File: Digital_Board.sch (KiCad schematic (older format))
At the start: 0 parts

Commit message: Rearranged the top sheet blocks modified hir. pins in few blocks
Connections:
- net labels added: 12V
- wire segments 23 -> 24

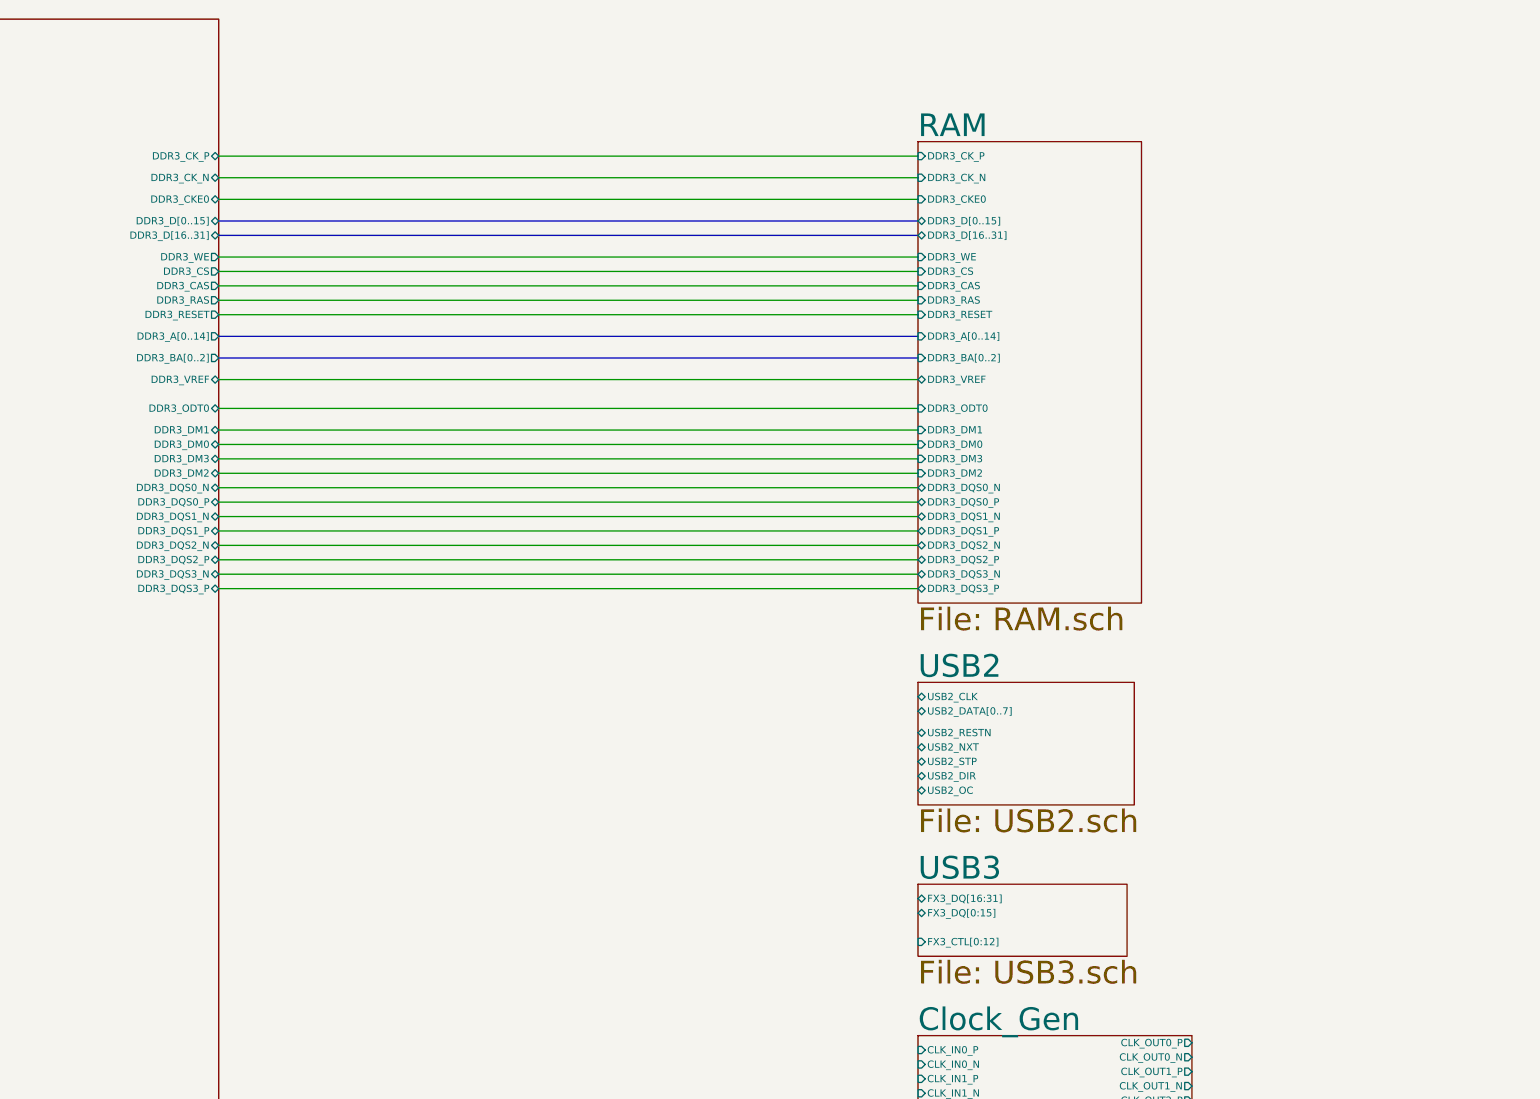
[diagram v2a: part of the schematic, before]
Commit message: Added nets for fx3 usb3 cct from fpga
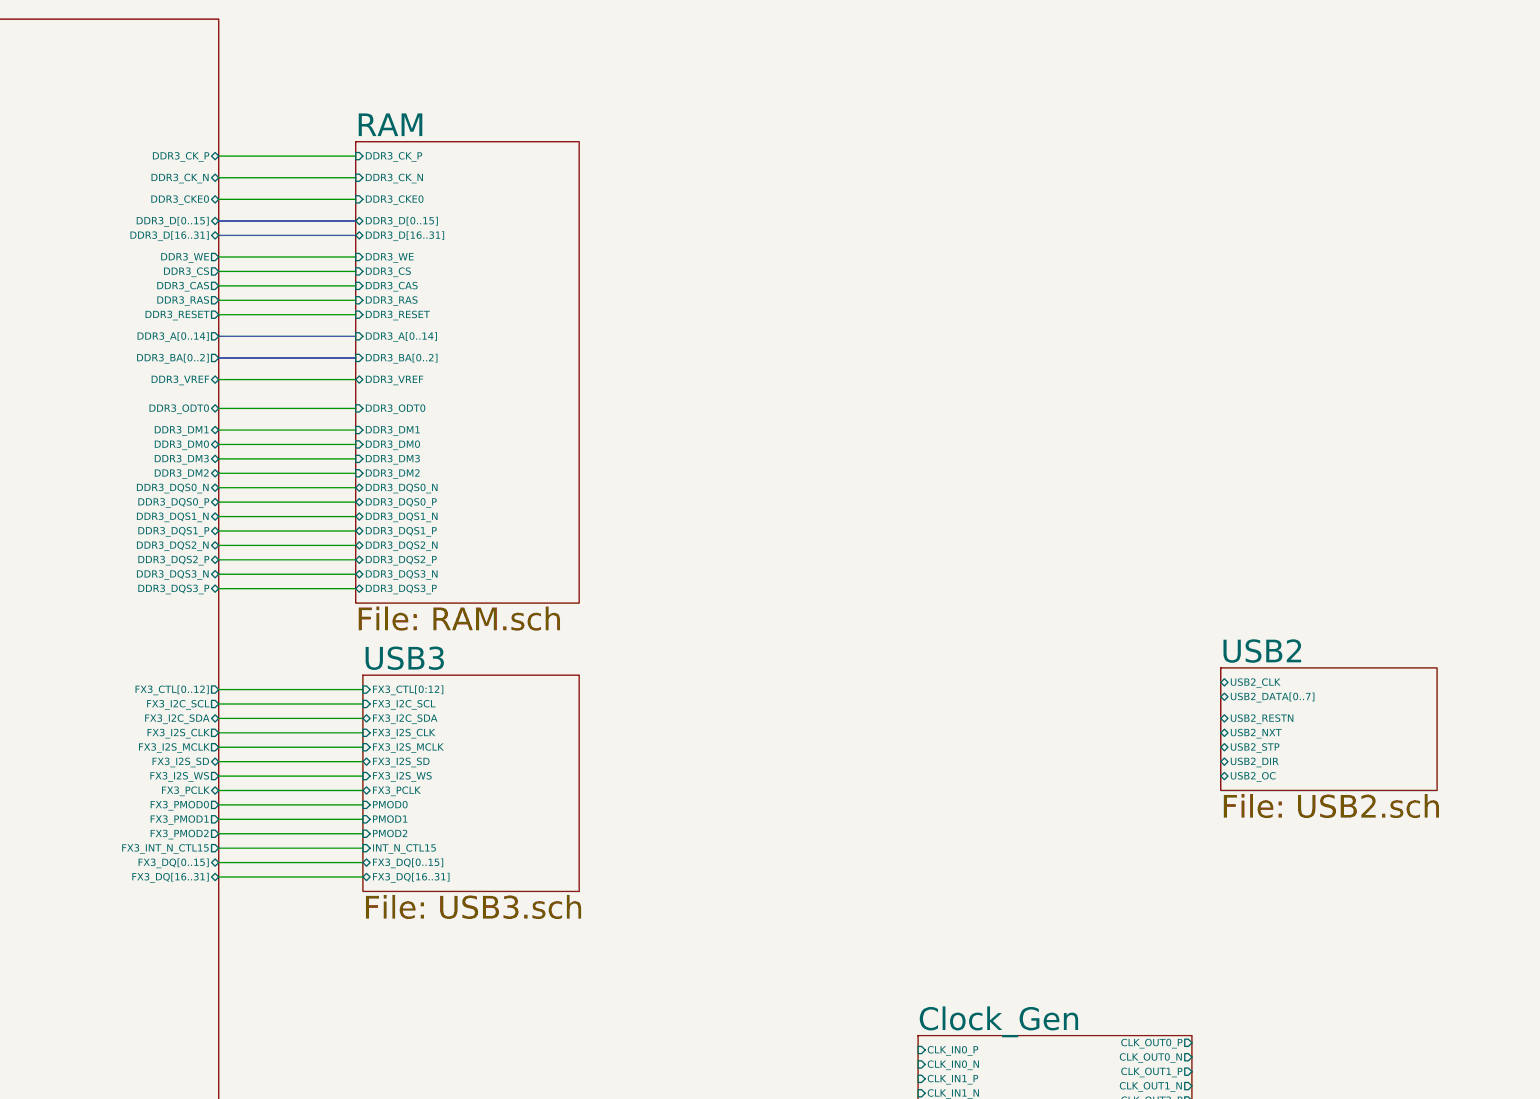
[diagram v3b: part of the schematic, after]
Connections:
- wire segments 24 -> 38
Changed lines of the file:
@@
 $EndSheet
 $Sheet
-S 19050 5350 1500 850
+S 21150 5250 1500 850
 U 601E7BF0
 F0 "USB2" 157
 F1 "USB2.sch" 157
-F2 "USB2_DATA[0..7]" B L 19050 5550 50
-F3 "USB2_DIR" B L 19050 6000 50
-F4 "USB2_STP" B L 19050 5900 50
-F5 "USB2_NXT" B L 19050 5800 50
-F6 "USB2_RESTN" B L 19050 5700 50
-F7 "USB2_CLK" B L 19050 5450 50
-F8 "USB2_OC" B L 19050 6100 50
+F2 "USB2_DATA[0..7]" B L 21150 5450 50
+F3 "USB2_DIR" B L 21150 5900 50
+F4 "USB2_STP" B L 21150 5800 50
+F5 "USB2_NXT" B L 21150 5700 50
+F6 "USB2_RESTN" B L 21150 5600 50
+F7 "USB2_CLK" B L 21150 5350 50
+F8 "USB2_OC" B L 21150 6000 50
 $EndSheet
 $Sheet
@@
 	3400 14750 4000 14750
 $Sheet
-S 19050 6750 1450 500
+S 15200 5300 1500 1500
 U 601E7BBE
 F0 "USB3" 157
 F1 "USB3.sch" 157
-F2 "FX3_DQ[16:31]" B L 19050 6850 50
-F3 "FX3_DQ[0:15]" B L 19050 6950 50
-F4 "FX3_CTL[0:12]" I L 19050 7150 50
+F2 "FX3_CTL[0:12]" I L 15200 5400 50
+F3 "FX3_I2C_SCL" I L 15200 5500 50
+F4 "FX3_I2C_SDA" B L 15200 5600 50
+F5 "FX3_PCLK" B L 15200 6100 50
+F6 "FX3_I2S_CLK" I L 15200 5700 50
+F7 "FX3_I2S_MCLK" I L 15200 5800 50
+F8 "PMOD0" I L 15200 6200 50
+F9 "PMOD1" I L 15200 6300 50
+F10 "PMOD2" I L 15200 6400 50
+F11 "INT_N_CTL15" I L 15200 6500 50
+F12 "FX3_DQ[16..31]" B L 15200 6700 50
+F13 "FX3_DQ[0..15]" B L 15200 6600 50
+F14 "FX3_I2S_SD" B L 15200 5900 50
+F15 "FX3_I2S_WS" I L 15200 6000 50
 $EndSheet
 $Sheet
@@
 F26 "DDR3_D[0..15]" B R 14200 2150 50
 F27 "DDR3_VREF" B R 14200 3250 50
+F28 "FX3_DQ[0..15]" B R 14200 6600 50
+F29 "FX3_DQ[16..31]" B R 14200 6700 50
+F30 "FX3_I2C_SDA" B R 14200 5600 50
+F31 "FX3_I2C_SCL" O R 14200 5500 50
+F32 "FX3_PCLK" B R 14200 6100 50
+F33 "FX3_I2S_CLK" O R 14200 5700 50
+F34 "FX3_I2S_MCLK" O R 14200 5800 50
+F35 "FX3_I2S_WS" O R 14200 6000 50
+F36 "FX3_I2S_SD" B R 14200 5900 50
+F37 "FX3_PMOD0" O R 14200 6200 50
+F38 "FX3_PMOD1" O R 14200 6300 50
+F39 "FX3_PMOD2" O R 14200 6400 50
+F40 "FX3_CTL[0..12]" O R 14200 5400 50
+F41 "FX3_INT_N_CTL15" O R 14200 6500 50
 $EndSheet
 Text Label 3650 14750 0    50   ~ 0
@@
 12V
 $Sheet
-S 19050 1600 1550 3200
+S 15150 1600 1550 3200
 U 601E7AEB
 F0 "RAM" 157
 F1 "RAM.sch" 157
-F2 "DDR3_CK_P" I L 19050 1700 50
-F3 "DDR3_CK_N" I L 19050 1850 50
-F4 "DDR3_CKE0" I L 19050 2000 50
-F5 "DDR3_CS" I L 19050 2500 50
-F6 "DDR3_RAS" I L 19050 2700 50
-F7 "DDR3_CAS" I L 19050 2600 50
-F8 "DDR3_WE" I L 19050 2400 50
-F9 "DDR3_BA[0..2]" I L 19050 3100 50
-F10 "DDR3_A[0..14]" I L 19050 2950 50
-F11 "DDR3_VREF" B L 19050 3250 50
-F12 "DDR3_RESET" I L 19050 2800 50
-F13 "DDR3_ODT0" I L 19050 3450 50
-F14 "DDR3_DM1" I L 19050 3600 50
-F15 "DDR3_DM0" I L 19050 3700 50
-F16 "DDR3_DM3" I L 19050 3800 50
-F17 "DDR3_DM2" I L 19050 3900 50
-F18 "DDR3_DQS0_N" B L 19050 4000 50
-F19 "DDR3_DQS0_P" B L 19050 4100 50
-F20 "DDR3_DQS1_N" B L 19050 4200 50
-F21 "DDR3_DQS1_P" B L 19050 4300 50
-F22 "DDR3_DQS2_N" B L 19050 4400 50
-F23 "DDR3_DQS2_P" B L 19050 4500 50
-F24 "DDR3_DQS3_N" B L 19050 4600 50
-F25 "DDR3_DQS3_P" B L 19050 4700 50
-F26 "DDR3_D[0..15]" B L 19050 2150 50
-F27 "DDR3_D[16..31]" B L 19050 2250 50
-$EndSheet
-Wire Wire Line
-	19050 3250 14200 3250
-Wire Wire Line
-	19050 4700 14200 4700
-Wire Wire Line
-	19050 4600 14200 4600
-Wire Wire Line
-	19050 4500 14200 4500
-Wire Wire Line
-	19050 4400 14200 4400
-Wire Wire Line
-	14200 4300 19050 4300
-Wire Wire Line
-	19050 4200 14200 4200
-Wire Wire Line
-	14200 4100 19050 4100
-Wire Wire Line
-	19050 4000 14200 4000
-Wire Wire Line
-	19050 3900 14200 3900
-Wire Wire Line
-	19050 3800 14200 3800
-Wire Wire Line
-	19050 3700 14200 3700
-Wire Wire Line
-	14200 3450 19050 3450
-Wire Wire Line
-	14200 3600 19050 3600
-Wire Wire Line
-	14200 1700 19050 1700
-Wire Wire Line
-	19050 1850 14200 1850
-Wire Wire Line
-	14200 2000 19050 2000
+F2 "DDR3_CK_P" I L 15150 1700 50
+F3 "DDR3_CK_N" I L 15150 1850 50
+F4 "DDR3_CKE0" I L 15150 2000 50
+F5 "DDR3_CS" I L 15150 2500 50
+F6 "DDR3_RAS" I L 15150 2700 50
+F7 "DDR3_CAS" I L 15150 2600 50
+F8 "DDR3_WE" I L 15150 2400 50
+F9 "DDR3_BA[0..2]" I L 15150 3100 50
+F10 "DDR3_A[0..14]" I L 15150 2950 50
+F11 "DDR3_VREF" B L 15150 3250 50
+F12 "DDR3_RESET" I L 15150 2800 50
+F13 "DDR3_ODT0" I L 15150 3450 50
+F14 "DDR3_DM1" I L 15150 3600 50
+F15 "DDR3_DM0" I L 15150 3700 50
+F16 "DDR3_DM3" I L 15150 3800 50
+F17 "DDR3_DM2" I L 15150 3900 50
+F18 "DDR3_DQS0_N" B L 15150 4000 50
+F19 "DDR3_DQS0_P" B L 15150 4100 50
+F20 "DDR3_DQS1_N" B L 15150 4200 50
+F21 "DDR3_DQS1_P" B L 15150 4300 50
+F22 "DDR3_DQS2_N" B L 15150 4400 50
+F23 "DDR3_DQS2_P" B L 15150 4500 50
+F24 "DDR3_DQS3_N" B L 15150 4600 50
+F25 "DDR3_DQS3_P" B L 15150 4700 50
+F26 "DDR3_D[0..15]" B L 15150 2150 50
+F27 "DDR3_D[16..31]" B L 15150 2250 50
+$EndSheet
+Wire Wire Line
+	15150 3250 14200 3250
+Wire Wire Line
+	15150 4700 14200 4700
+Wire Wire Line
+	15150 4600 14200 4600
+Wire Wire Line
+	15150 4500 14200 4500
+Wire Wire Line
+	15150 4400 14200 4400
+Wire Wire Line
+	14200 4300 15150 4300
+Wire Wire Line
+	15150 4200 14200 4200
+Wire Wire Line
+	14200 4100 15150 4100
+Wire Wire Line
+	15150 4000 14200 4000
+Wire Wire Line
+	15150 3900 14200 3900
+Wire Wire Line
+	15150 3800 14200 3800
+Wire Wire Line
+	15150 3700 14200 3700
+Wire Wire Line
+	14200 3450 15150 3450
+Wire Wire Line
+	14200 3600 15150 3600
+Wire Wire Line
+	14200 1700 15150 1700
+Wire Wire Line
+	15150 1850 14200 1850
+Wire Wire Line
+	14200 2000 15150 2000
 Wire Bus Line
-	19050 2150 14200 2150
+	15150 2150 14200 2150
 Wire Bus Line
-	14200 2250 19050 2250
-Wire Wire Line
-	19050 2800 14200 2800
-Wire Wire Line
-	14200 2700 19050 2700
-Wire Wire Line
-	19050 2600 14200 2600
-Wire Wire Line
-	14200 2500 19050 2500
-Wire Wire Line
-	19050 2400 14200 2400
+	14200 2250 15150 2250
+Wire Wire Line
+	15150 2800 14200 2800
+Wire Wire Line
+	14200 2700 15150 2700
+Wire Wire Line
+	15150 2600 14200 2600
+Wire Wire Line
+	14200 2500 15150 2500
+Wire Wire Line
+	15150 2400 14200 2400
 Wire Bus Line
-	19050 2950 14200 2950
+	15150 2950 14200 2950
 Wire Bus Line
-	19050 3100 14200 3100
+	15150 3100 14200 3100
+Wire Wire Line
+	14200 5400 15200 5400
+Wire Wire Line
+	14200 5500 15200 5500
+Wire Wire Line
+	14200 5600 15200 5600
+Wire Wire Line
+	14200 5700 15200 5700
+Wire Wire Line
+	14200 5800 15200 5800
+Wire Wire Line
+	14200 5900 15200 5900
+Wire Wire Line
+	14200 6000 15200 6000
+Wire Wire Line
+	14200 6100 15200 6100
+Wire Wire Line
+	14200 6200 15200 6200
+Wire Wire Line
+	14200 6300 15200 6300
+Wire Wire Line
+	14200 6400 15200 6400
+Wire Wire Line
+	14200 6500 15200 6500
+Wire Wire Line
+	14200 6600 15200 6600
+Wire Wire Line
+	14200 6700 15200 6700
 $EndSCHEMATC
